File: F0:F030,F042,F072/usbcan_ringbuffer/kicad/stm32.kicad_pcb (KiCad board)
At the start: 2 copper layers, 64.5 x 26 mm, 59 parts, among them J1 Screw_Terminal_01x03, J10 SDA, J11 PB0, J12 PB1, J13 PB4, J14 PB5, J15 PB2, J16 PB3, J17 GND, J18 GND, J19 +3.3V, J2 SCK, J20 +5V, J21 PA0, J22 PA1, J23 PA2, J24 PA3, J25 PB10, J26 PB11, J27 PB12, J28 PB13, J29 PB14, J3 SWDetc, J30 PA4, J31 GND, J4 USB_B, J5 MISO, J6 MOSI, J7 TX, J8 RX, J9 SCL, P1 Hole, P2 Hole, P3 Hole, P4 Hole, Q1 B0505S, SW1 SW_DIP_x01, U1 LM1117-3.3, U2 USBLC6-2SC6, U3 STM32F072C8Tx, U4 ISO1050DUB

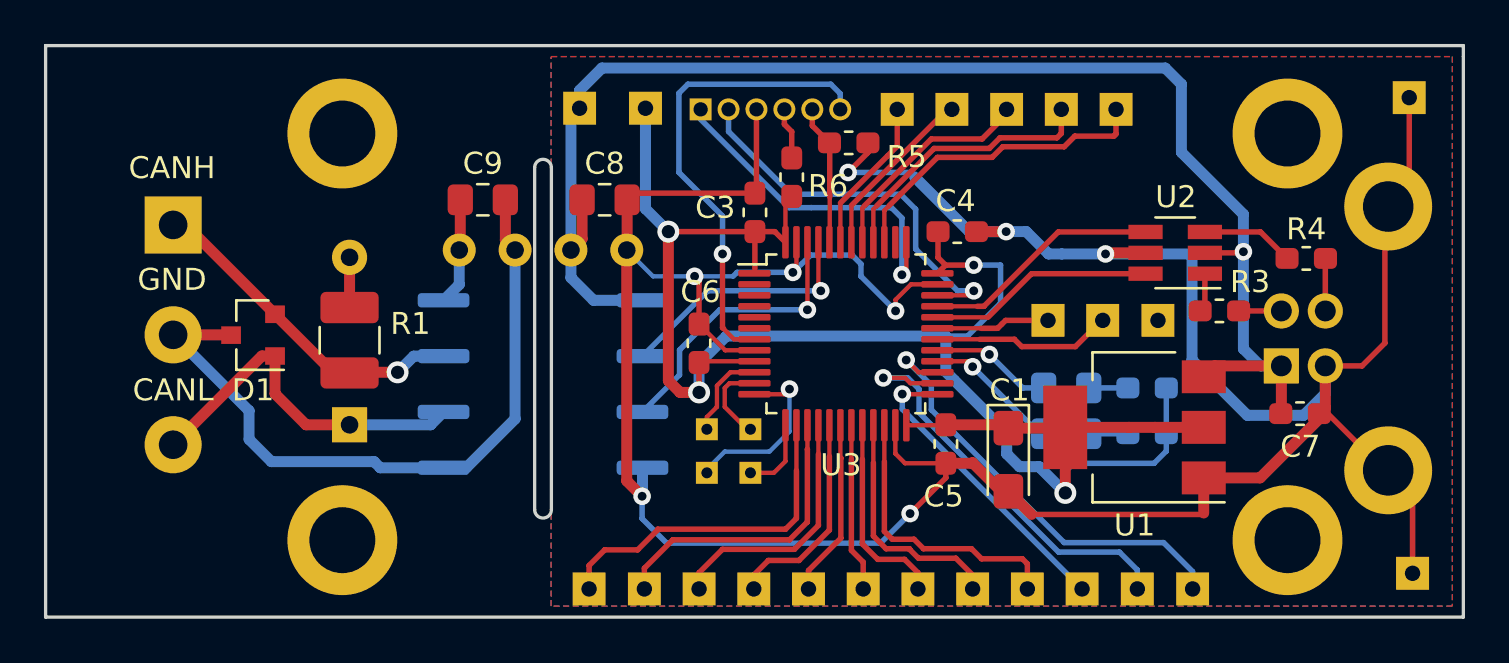
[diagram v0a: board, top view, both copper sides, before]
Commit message: fixed bug with usblc6 on usbcan
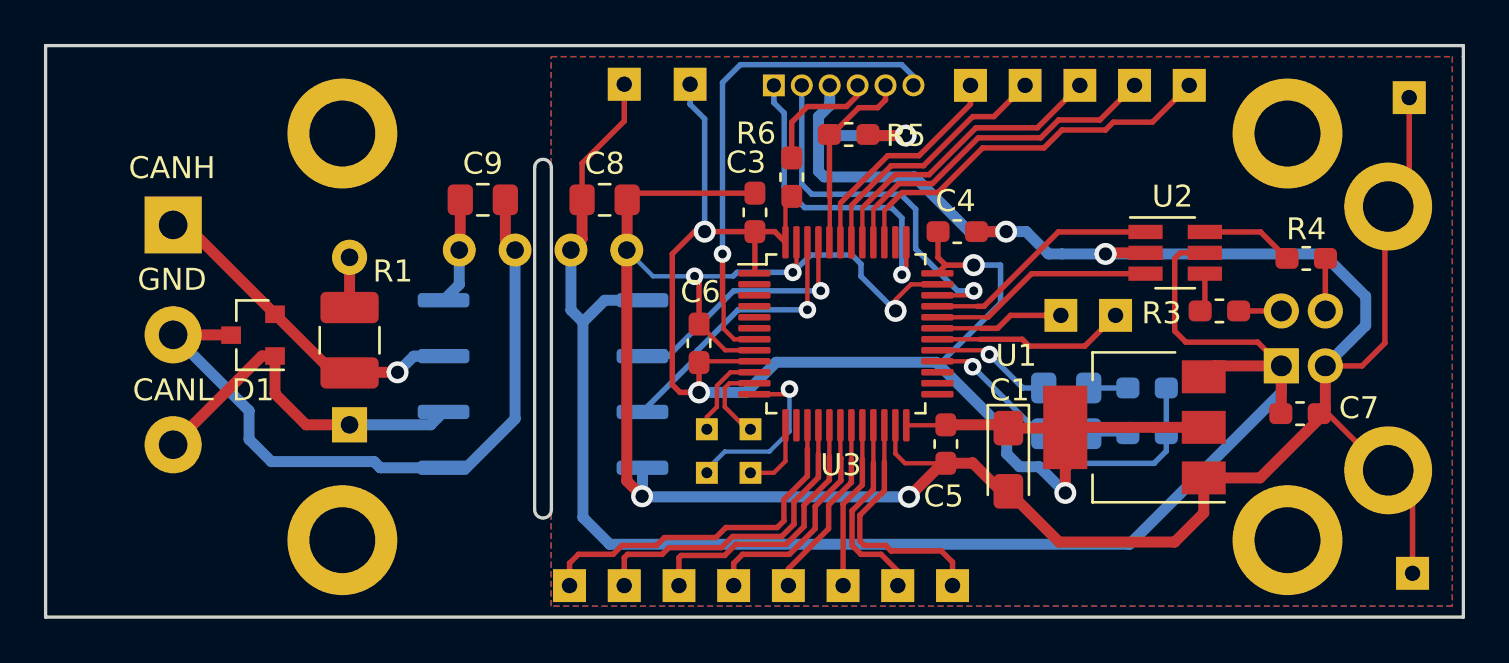
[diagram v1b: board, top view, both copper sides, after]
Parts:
- removed J27: PB12, TestPoint:TestPoint_THTPad_1.5x1.5mm_Drill0.7mm
- removed J28: PB13, TestPoint:TestPoint_THTPad_1.5x1.5mm_Drill0.7mm
- removed J29: PB14, TestPoint:TestPoint_THTPad_1.5x1.5mm_Drill0.7mm
- removed J30: PA4, TestPoint:TestPoint_THTPad_1.5x1.5mm_Drill0.7mm
- removed J31: GND, TestPoint:TestPoint_THTPad_1.5x1.5mm_Drill0.7mm
- moved J13 3.51 mm to (110.5, 51.3)
- moved J16 3.51 mm to (113.0, 51.3)
- moved J3 3.51 mm to (94.1, 51.3)
- moved J10 3.51 mm to (103.1, 51.3)
- moved J14 3.51 mm to (108.1, 51.3)
- moved J9 3.51 mm to (105.6, 51.3)
- moved J25 3.41 mm to (99.8, 74.1)
- moved J5 3.41 mm to (87.3, 74.1)
- moved J11 3.41 mm to (92.3, 74.1)
- moved J12 3.41 mm to (94.8, 74.1)
- moved J15 3.41 mm to (97.3, 74.1)
- moved J2 3.41 mm to (84.8, 74.1)
- moved J26 3.41 mm to (102.3, 74.1)
- moved J6 3.41 mm to (89.8, 74.1)
- moved J19 2.31 mm to (90.3, 51.3)
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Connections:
- U2 pad 1: Net-(R3-Pad2) -> Net-(U2-Pad1)
- U2 pad 2: +5V -> GND
- U2 pad 3: Net-(R4-Pad2) -> Net-(U2-Pad3)
- U2 pad 4: Net-(U2-Pad4) -> Net-(R3-Pad2)
- U2 pad 5: GND -> +5V
- U2 pad 6: Net-(U2-Pad6) -> Net-(R4-Pad2)
- U3 pad 14: Net-(U3-Pad14) -> unconnected-(U3-Pad14)
- U3 pad 25: Net-(U3-Pad25) -> unconnected-(U3-Pad25)
- U3 pad 26: Net-(U3-Pad26) -> unconnected-(U3-Pad26)
- U3 pad 27: Net-(U3-Pad27) -> unconnected-(U3-Pad27)
- U3 pad 32: Net-(U2-Pad6) -> Net-(U2-Pad3)
- U3 pad 33: Net-(U2-Pad4) -> Net-(U2-Pad1)
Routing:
- net Net-(U3-Pad27): track 20.1 -> 0.00 mm, vias 1 -> 0
- net Net-(U3-Pad26): track 19.2 -> 0.00 mm, vias 1 -> 0
- net Net-(U3-Pad14): track 15.6 -> 0.00 mm
- net Net-(U3-Pad25): track 13.9 -> 0.00 mm, vias 1 -> 0
- net Net-(U2-Pad4): track 10.9 -> 0.00 mm
- net Net-(U2-Pad1): track 0.00 -> 10.9 mm
- net +5V: track 65.9 -> 76.6 mm, vias 1 -> 0
- net Net-(U2-Pad3): track 0.00 -> 10.3 mm
- net Net-(U2-Pad6): track 10.3 -> 0.00 mm
- net Net-(J9-Pad1): track 8.06 -> 11.8 mm
- net Net-(J14-Pad1): track 10.1 -> 13.8 mm
- net Net-(J10-Pad1): track 7.12 -> 10.4 mm
- net Net-(J3-Pad4): track 2.35 -> 5.59 mm
- net Net-(J13-Pad1): track 12.6 -> 15.7 mm
- net Net-(J16-Pad1): track 14.6 -> 17.7 mm
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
